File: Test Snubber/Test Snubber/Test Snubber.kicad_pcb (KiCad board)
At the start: 2 copper layers, 54.4 x 23 mm, 22 parts, among them J1 1702473, J2 1702473, U1 AP63357QZV-7

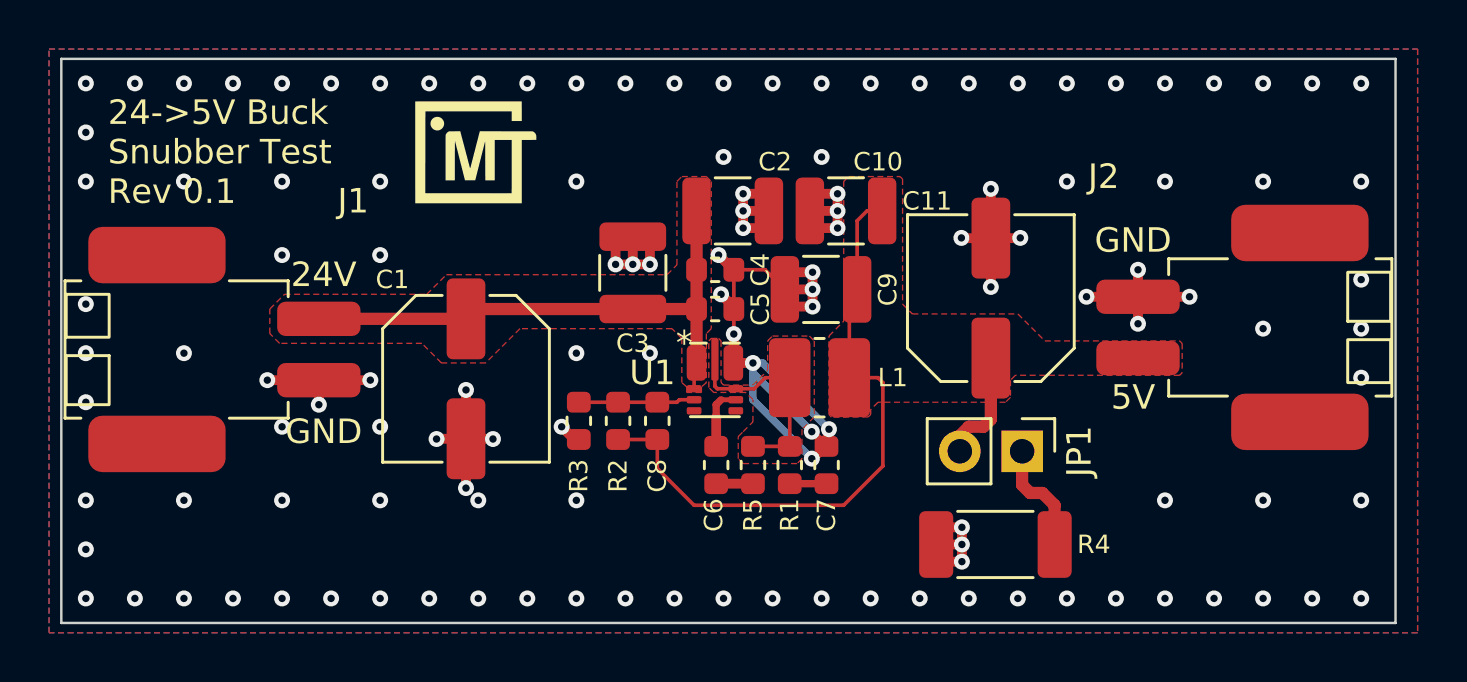
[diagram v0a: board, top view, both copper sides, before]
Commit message: Finishes Test Snubber board
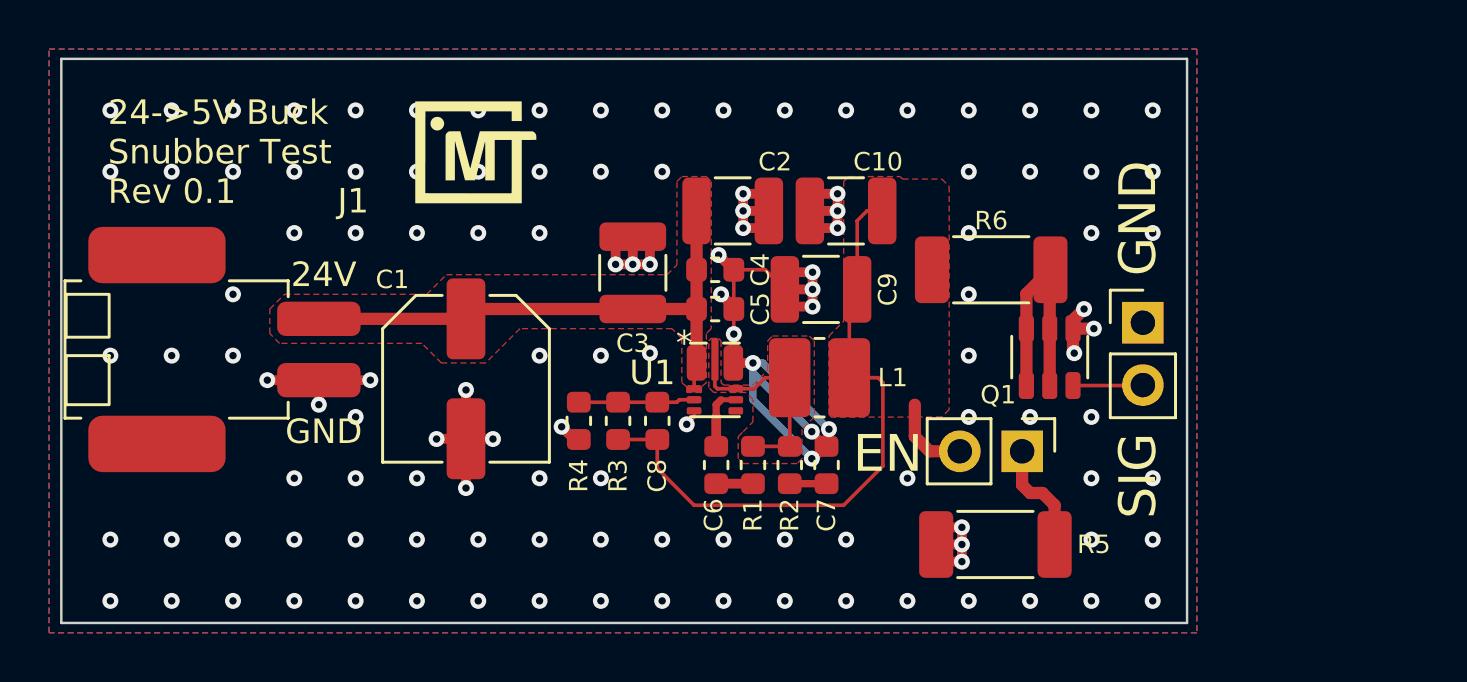
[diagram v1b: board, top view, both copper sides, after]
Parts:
- removed C11: EEE-1VA470WP, footprints:CAPAE660X580L260X65N
- removed J2: 1702473, footprints:1702473
- added JP2: Jumper_NO_Small, Connector_PinHeader_2.54mm:PinHeader_1x02_P2.54mm_Vertical, F.Cu at (116.2, 57.8)
- added Q1: SI1442DH-T1-GE3, footprints:SOT23-6P95_285X140L45X42N, F.Cu at (112.4, 59.2)
- added R6: 35028R2JT, footprints:RESISTOR_2010N, F.Cu at (110.0, 55.6)
- renumbered R5 to R1, R1 to R2, R2 to R3, R3 to R4, R4 to R5
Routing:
- net Net-(Q1-Pad1): track 0.00 -> 9.86 mm
- net GND: track 72.0 -> 62.7 mm
- net Net-(JP2-Pad2): track 0.00 -> 2.86 mm
- net +5V: track 30.5 -> 29.2 mm
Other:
- board size 54.4 x 23 mm -> 45.9 x 23 mm
- board text added: "EN"
- board text added: "SIG"
- board text removed: "5V"
